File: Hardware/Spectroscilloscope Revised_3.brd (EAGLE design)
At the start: 74.9 x 181.3 mm, 52 parts, among them IC1 7805TV, Q1 16MHz, U1 ATMEGA328P-PU, U2 MCP6024-I/P, U3 MCP6024-I/P

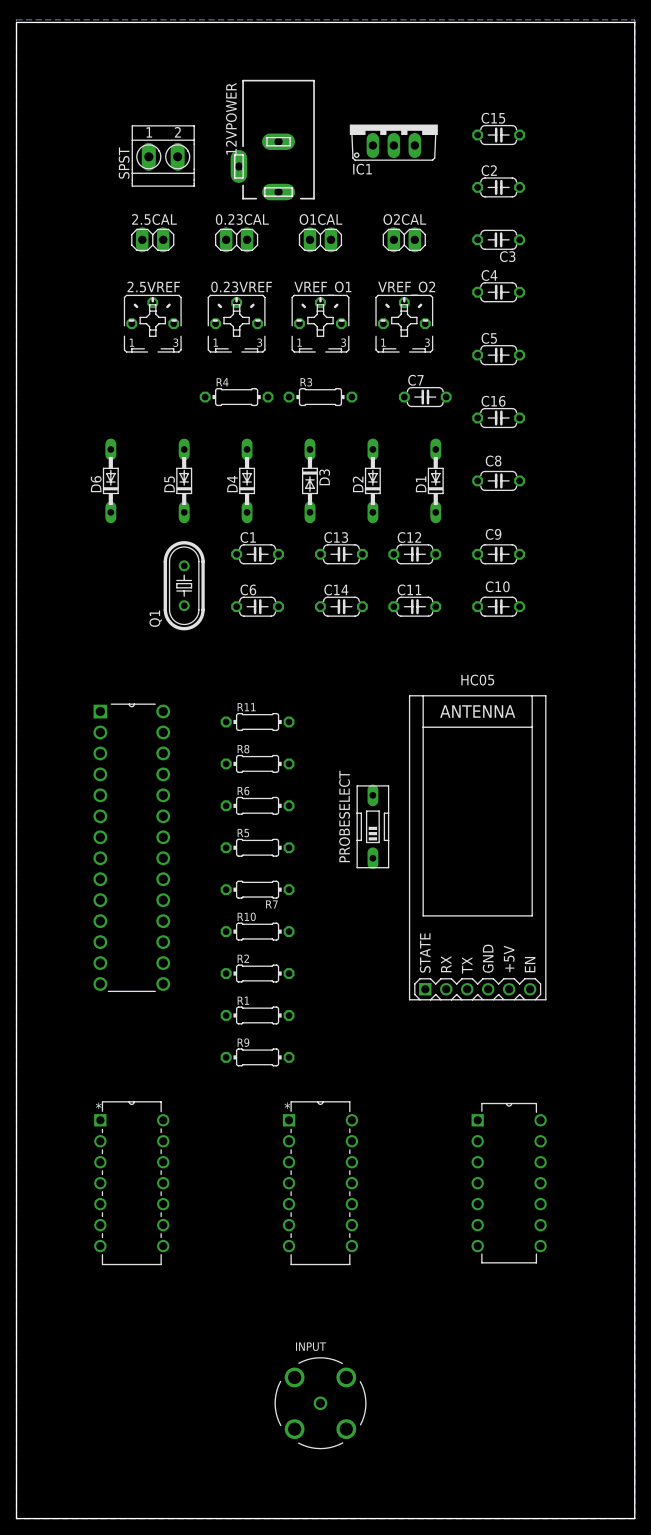
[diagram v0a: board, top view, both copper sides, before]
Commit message: Revised the Front end design - Final revision - multisim simulation works - Testing Breadboard April 21
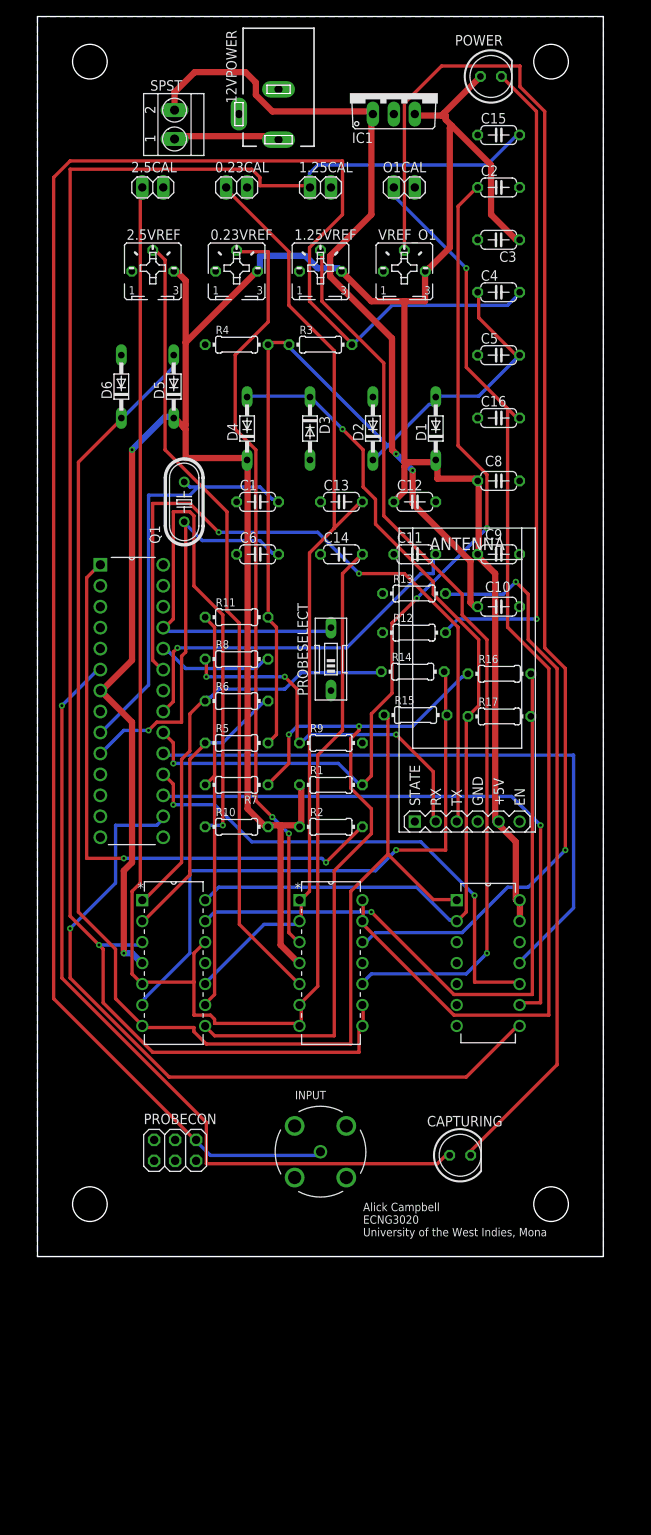
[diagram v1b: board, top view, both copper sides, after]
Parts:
- removed C7: 0.1u, rcl:C050-024X044
- removed O2CAL: (no value), pinhead:1X02
- removed VREF_O2: 100k, pot:B25P
- added 1.25CAL: (no value), pinhead:1X02
- added 1.25VREF: 100k, pot:B25P
- added CAPTURING, POWER: (no value), led:LED5MM
- added PROBECON: (no value), pinhead:2X03
- added R12, R13: 330, rcl:0204/7
- added R14, R15, R16, R17: 1k, rcl:0204/7
- moved R9 39.1 mm to (38.1, 94.0)
- moved INPUT 30.5 mm to (36.8, 44.5)
- moved R1 29.3 mm to (38.1, 88.9)
- moved U2 27.1 mm to (22.9, 59.7)
- moved U$1 26.8 mm to (61.0, 59.7)
- moved U3 26.7 mm to (41.9, 59.7)
- moved PROBESELECT 20.9 mm to (38.1, 104.1)
- moved HC05 20.4 mm to (54.6, 101.6)
- moved R2 19.9 mm to (38.1, 83.8)
- moved U1 17.8 mm to (17.8, 82.5)
- moved R11 13.0 mm to (26.7, 109.2)
- moved R5 13.0 mm to (26.7, 94.0)
- moved R6 13.0 mm to (26.7, 99.1)
- moved R7 13.0 mm to (26.7, 88.9)
- moved R8 13.0 mm to (26.7, 104.1)
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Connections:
- removed net N$11: R8.2, U1.3
- removed net NONINV: C4.1, C5.2, D1.A, D2.C, R3.1, R4.2, R6.2, U2.3
- removed net VREF_O2: C16.2, O2CAL.1, U3.13, U3.14
- new net 1.25VREF: 1.25CAL.1, C15.2, U2.3, U3.8, U3.9
- new net CAPTURING: CAPTURING.A, U1.6
- new net COMPANDED: C4.1, C5.2, D1.A, D2.C, R11.2, R3.1, R4.2, R5.2
- new net N$12: POWER.K, R12.2
- new net N$13: CAPTURING.K, R13.2
- new net N$15: R14.2, R15.2, U2.6
- new net N$17: R8.2, U1.24
- new net N$21: R16.2, R17.2, U2.13
- new net N$22: R16.1, R7.1, U2.8
- net +12VI: now also 12VPOWER.1; no longer 12VPOWER.2, 12VPOWER.3
- net 0.23VREF: now also U2.10; no longer U2.5
- net 2.5VREF: now also U2.12, U2.5; no longer C7.2, R4.1, U2.10
- net GND: now also 1.25CAL.2, 1.25VREF.A, 12VPOWER.2, 12VPOWER.3, PROBECON.1, PROBECON.2, PROBECON.3, PROBECON.4, PROBECON.5, R12.1, R13.1, R4.1; no longer 12VPOWER.1, C7.1, O2CAL.2, VREF_O2.A
- net N$10: now also VREF_O1.S; no longer VREF_O2.S
- net N$16: now also R11.1, R7.2; no longer R11.2, R5.1
- net N$4: now also R14.1, R6.1, U2.1; no longer R5.2, R7.1, U2.7
- net N$5: now also R5.1, R6.2, U2.2; no longer R6.1, R7.2, U2.6
- net N$7: now also 1.25VREF.S; no longer VREF_O1.S
- net TX: now also U1.23; no longer U1.2
- net VCC: now also 1.25VREF.E, POWER.A; no longer VREF_O2.E
- net VIN: now also PROBECON.6
- net VREF_O1: now also C16.2, U3.13, U3.14; no longer C15.2, U3.8, U3.9
- net X1: now also R15.1, U2.7; no longer U2.1, U2.2
- net X10: now also R17.1, U2.14; no longer R11.1, U2.8
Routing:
- net VCC: track 0.00 -> 359.9 mm, vias 0 -> 2
- net VIN: track 0.00 -> 224.8 mm
- net 1.25VREF: track 0.00 -> 207.3 mm, vias 0 -> 1
- net 2.5VREF: track 0.00 -> 187.4 mm
- net X1: track 0.00 -> 168.3 mm
- net N$10: track 0.00 -> 160.2 mm, vias 0 -> 1
- net VREF_O1: track 0.00 -> 140.0 mm, vias 0 -> 1
- net 0.23VREF: track 0.00 -> 115.6 mm
- net X10: track 0.00 -> 113.6 mm, vias 0 -> 1
- net N$7: track 0.00 -> 110.2 mm, vias 0 -> 1
- net N$8: track 0.00 -> 109.3 mm, vias 0 -> 3
- net COMPANDED: track 0.00 -> 102.8 mm
- net +12V: track 0.00 -> 99.7 mm, vias 0 -> 2
- net CAPTURING: track 0.00 -> 99.2 mm, vias 0 -> 1
- net N$3: track 0.00 -> 96.4 mm
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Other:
- board size 74.9 x 181.3 mm -> 68.6 x 150.2 mm
- board text added: "Alick Campbell ECNG3020 University of the West Indies, Mona"
